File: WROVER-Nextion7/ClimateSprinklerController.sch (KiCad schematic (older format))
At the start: 220 parts, among them J1 7.5 TO 40 V, J10 HVAC, J11 RELAY, J2 USB_B_Micro, J3 POWER SEL, J4 NEXTION, J5 SERIAL, J6 SPI, J7 PIR, J8 I2C, J9 IO_EXP, K1 G6E-134P-US DC5, K2 G6E-134P-US DC5, K3 G6E-134P-US DC5, Q1 MMSS8050, Q10 2N6073B, Q11 2N6073B, Q12 2N6073B, Q13 2N6073B, Q14 2N6073B, Q2 MMSS8050, Q3 TEPT5700, Q4 2N7002, Q5 2N7002, Q6 2N7002, Q7 2N6073B, Q8 2N6073B, Q9 2N6073B, SW1 POWER, SW2 RESET, SW3 MODE, U1 ESP32-WROVER, U10 SHTC3, U11 TMP117, U12 MOC3043, U13 MOC3043, U14 MOC3043, U15 MOC3043, U16 MOC3043, U17 MOC3043, U18 MOC3043, U19 MOC3043, U2 MCP23017_SO, U20 DHT22, U3 FT232RL, U4 TPS22917DBV, U5 LMR36520, U6 SGP40-Sensor_Air_Quality, U7 BME680, U8 LD1086DT33TR, U9 BME280

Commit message: Nextion PCBs tweak
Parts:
- R12, R20: Part RC0805FR-07100KL -> RC0805FR-074R7L
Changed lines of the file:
@@
 F 2 "Resistor_SMD:R_0805_2012Metric_Pad1.20x1.40mm_HandSolder" V 9180 12150 50  0001 C CNN
 F 3 "~" H 9250 12150 50  0001 C CNN
-F 4 "RC0805FR-07100KL" H 9250 12150 50  0001 C CNN "Part"
+F 4 "RC0805FR-074R7L" H 9250 12150 50  0001 C CNN "Part"
 	1    9250 12150
 	1    0    0    -1
@@
 F 2 "Resistor_SMD:R_0805_2012Metric_Pad1.20x1.40mm_HandSolder" V 5980 4700 50  0001 C CNN
 F 3 "~" H 6050 4700 50  0001 C CNN
-F 4 "RC0805FR-07100KL" H 6050 4700 50  0001 C CNN "Part"
+F 4 "RC0805FR-074R7L" H 6050 4700 50  0001 C CNN "Part"
 	1    6050 4700
 	-1   0    0    1

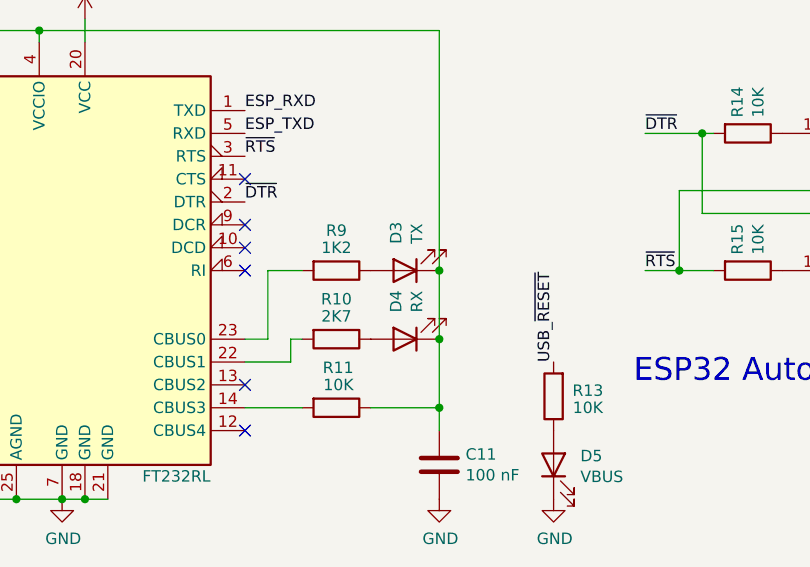
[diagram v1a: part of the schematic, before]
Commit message: TX+RX LEDs were backwards...oops
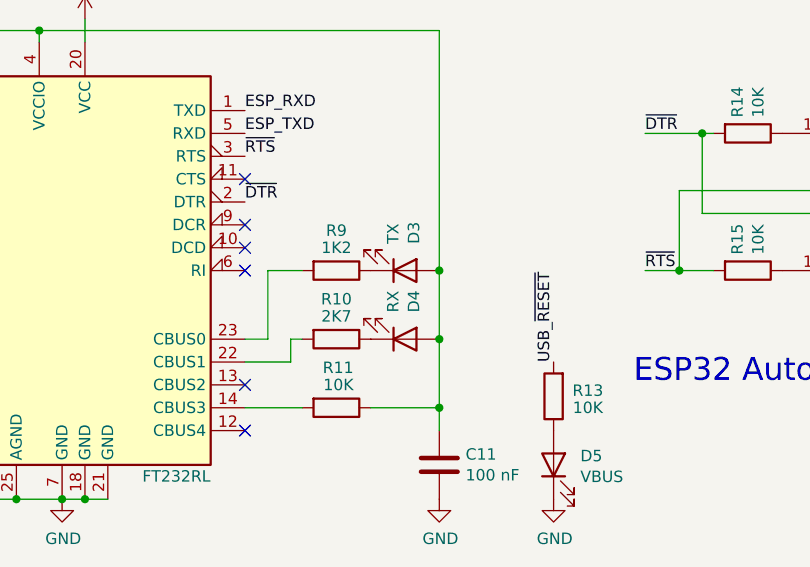
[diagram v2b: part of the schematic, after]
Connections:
- net at C11.1, R11.1, U3.17 (3V3OUT)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: now also D3.2 (A), D4.2 (A); no longer D3.1 (K), D4.1 (K)
- net at R9.1: now also D3.1 (K); no longer D3.2 (A)
- net at R10.1: now also D4.1 (K); no longer D4.2 (A)
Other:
- moved on the sheet: D3, D4
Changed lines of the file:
@@
 F 4 "APTL3216QBC/D" V 5850 12900 50  0001 C CNN "Part"
 	1    5850 12900
-	-1   0    0    1
+	1    0    0    1
 $EndComp
 $Comp
@@
 F 4 "APTL3216SURCK" V 5850 13200 50  0001 C CNN "Part"
 	1    5850 13200
-	-1   0    0    1
+	1    0    0    1
 $EndComp
 Wire Wire Line

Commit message: Doc updates, new images, new enclosures, regenerate gerbers
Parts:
- C1: MPN1 (none) -> C2012X5R1V106K085AC; Part C2012X5R1V106K085AC -> (none)
- C10, C11, C15, C17, C22, C23, C24, C27, C28, C29, C3, C30, C31, C32, C4, C6, C8: MPN1 (none) -> CC0805KRX7R7BB104; Part CC0805KRX7R7BB104 -> (none)
- C12, C2, C5, C9: MPN1 (none) -> C2012X5R1H475K125AB; Part C2012X5R1H475K125AB -> (none)
- C13: MPN1 (none) -> C2012X5R1H224K125AA; Part C2012X5R1H224K125AA -> (none)
- C14, C19, C20: MPN1 (none) -> C0805C105K4RACTU; Part C0805C105K4RACTU -> (none)
- C16, C18, C21: MPN1 (none) -> GRM32ER61C476KE15L; Part GRM32ER61C476KE15L -> (none)
- C25, C26: MPN1 (none) -> EEE-HP0J100R; Part EEE-HP0J100R -> (none)
- C33, C34, C35, C36, C37, C38, C39, C40: MPN1 (none) -> CC0805KRX7R9BB103; Part CC0805KRX7R9BB103 -> (none)
- C7: MPN1 (none) -> UVK1H471MPD; Part UVK1H471MPD -> (none)
- D1: value MBR230S1F-7 -> N/A; MPN1 (none) -> MBR230S1F-7; Part MBR230S1F-7 -> (none)
- D10, D12, D14: MPN1 (none) -> APTL3216CGCK; Part APTL3216CGCK -> (none)
- D11, D13, D9: value 1N4148 -> N/A; MPN1 (none) -> 1N4148W; Part 1N4148W -> (none)
- D15, D5: MPN1 (none) -> APTL3216ZGC; Part APTL3216ZGC -> (none)
- D16, D17, D3: MPN1 (none) -> APTL3216QBC/D; Part APTL3216QBC/D -> (none)
- D18, D19, D4: MPN1 (none) -> APTL3216SURCK; Part APTL3216SURCK -> (none)
- D2: value CD-MBL206SL -> N/A; MPN1 (none) -> CD-MBL206SL; Part CD-MBL206SL -> (none)
- D20, D21, D22: MPN1 (none) -> APTL3216SYCK; Part APTL3216SYCK -> (none)
- D6, D7: MPN1 (none) -> 597-6901-607F; Part 597-6901-607F -> (none)
- D8: MPN1 (none) -> APTL3216SECK; Part APTL3216SECK -> (none)
- F1: MPN1 (none) -> 2920L030DR; Part 2920L030DR -> (none)
- H1, H10, H11, H12, H13, H14, H2, H3, H4, H5, H6, H7, H8, H9, J3, J4, J5, J6, J7, J8, J9, JP1, JP10, JP11, JP12, JP13, JP14, JP15, JP16, JP17, JP2, JP3, JP4, JP5, JP6, JP7, JP8, JP9: MPN1 (none) -> N/A; Population (none) -> DNF
- J1: MPN1 (none) -> 694106301002; Part 694106301002 -> (none)
- J10, J11: MPN1 (none) -> 1862039; Part 1862039 -> (none)
- J2: value USB_B_Micro -> N/A; MPN1 (none) -> 105017-0001; Part 105017-0001 -> (none)
- K1, K2, K3: MPN1 (none) -> G6E-134P-US DC5
- L1: MPN1 (none) -> 7447709150; MPN2 (none) -> MSS1210-153MEB; Part 7447709150 -> (none); PartAlt MSS1210-153MEB -> (none)
- Q1, Q2: MPN1 (none) -> MMSS8050; Part MMSS8050 -> (none)
- Q10, Q11, Q12, Q13, Q14, Q7, Q8, Q9: MPN1 (none) -> 2N6073BG; Part 2N6073BG -> (none)
- Q3: MPN1 (none) -> TEPT5700; Part TEPT5700 -> (none)
- Q4, Q5, Q6: MPN1 (none) -> 2N7002; Part 2N7002 -> (none)
- R1, R11, R14, R15, R2, R22, R25, R27, R3, R5, R6, R64, R7, R8: MPN1 (none) -> RC0805FR-0710KL; Part RC0805FR-0710KL -> (none)
- R10, R35, R36, R9: MPN1 (none) -> RT0805FRE072K7L; Part RT0805FRE072K7L -> (none)
- R12, R20: MPN1 (none) -> RC0805FR-074R7L; Part RC0805FR-074R7L -> (none)
- R13, R32: MPN1 (none) -> RC0805FR-0710KL; Part RT0805FRE079K1L -> (none)
- R16, R19: MPN1 (none) -> RC0805FR-07100KL; Part RC0805FR-07100KL -> (none)
- R17: MPN1 (none) -> RT0805FRE0724K9L; Part RT0805FRE0724K9L -> (none)
- R18, R21: MPN1 (none) -> RT0805FRE073K3L; Part RT0805FRE073K3L -> (none)
- R23: MPN1 (none) -> CRCW08055K00JNTA; Part CRCW08055K00JNTA -> (none)
- R24: MPN1 (none) -> RT0805FRE078K2L; Part RT0805FRE078K2L -> (none)
- R26: MPN1 (none) -> RT0805FRE071K6L; Part RT0805FRE071K6L -> (none)
- R28: MPN1 (none) -> RT0805FRE07120RL; Part RT0805FRE07120RL -> (none)
- R29, R30, R31: value 1K2 -> 560; MPN1 (none) -> RT0805FRE07560RL; Part RT0805FRE071K2L -> (none)
- R33, R34, R37, R38, R39: value 1K2 -> 1K5; MPN1 (none) -> RT0805FRE071K5L; Part RT0805FRE072K7L -> (none)
- R4: MPN1 (none) -> RT0805FRE074K7L; Part RT0805FRE074K7L -> (none)
- R40, R41, R42, R43, R44, R45, R46, R47: MPN1 (none) -> RT0805FRE07270RL; Part RT0805FRE07270RL -> (none)
- R48, R49, R50, R51, R52, R53, R54, R55: MPN1 (none) -> RT0805FRE07180RL; Part RT0805FRE07180RL -> (none)
- R56, R57, R58, R59, R60, R61, R62, R63: MPN1 (none) -> RT0805FRE07820RL; Part RT0805FRE07820RL -> (none)
- R65, R66, R67, R68, R69, R70, R71, R72: MPN1 (none) -> ERJ-P06J390V; Part ERJ-P06J390V -> (none)
- RV1: value B72205S0400K101 -> N/A; MPN1 (none) -> B72205S0400K101; Part B72205S0400K101 -> (none)
- SW1: MPN1 (none) -> 48BFSP1M6QT; Part 48BFSP1M6QT -> (none)
- SW2, SW3: MPN1 (none) -> PTS645VK582LFS; Part PTS645VK582LFS -> (none)
- TH1: value NXFT15XH103FA2B100 -> 10K; MPN1 (none) -> NXFT15XH103FA2B100; Part NXFT15XH103FA2B100 -> (none)
- U1: MPN1 (none) -> ESP32-WROVER; Part ESP32-WROVER -> (none)
- U10: MPN1 (none) -> SHTC3; Part SHTC3 -> (none)
- U11: value TMP117 -> TMP117MAIDRVR; MPN1 (none) -> TMP117MAIDRVR; Part TMP117MAIDRVR -> (none)
- U12, U13, U14, U15, U16, U17, U18, U19: value MOC3043 -> MOC3043SM; MPN1 (none) -> MOC3043SM; Part MOC3043SM -> (none)
- U2: value MCP23017_SO -> MCP23017-E/SO; MPN1 (none) -> MCP23017-E/SO; Part MCP23017-E/SO -> (none)
- U20: MPN1 (none) -> DHT22; Part DHT22 -> (none)
- U3: MPN1 (none) -> FT232RL; Part FT232RL -> (none)
- U4: MPN1 (none) -> TPS22917DBV; Part TPS22917DBV -> (none)
- U5: value LMR36520 -> LMR36520ADDAR; MPN1 (none) -> LMR36520ADDAR; Part LMR36520ADDAR -> (none)
- U6: value SGP40-Sensor_Air_Quality -> SGP40; MPN1 (none) -> SGP40; Part SGP40 -> (none)
- U7: MPN1 (none) -> BME680; Part BME680 -> (none)
- U8: MPN1 (none) -> LD1086DT33TR; Part LD1086DT33TR -> (none)
- U9: MPN1 (none) -> BME280; Part BME280 -> (none)
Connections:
- net +3V3: now also C32.1, U20.1 (VCC)
- net +5V: no longer C32.1, U20.1 (VCC)
